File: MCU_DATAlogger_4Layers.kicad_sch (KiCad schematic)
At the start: 25 parts, among them U1 24LC1025, U2 24LC1025, U3 ATMEGA328P-AU, U4 DS1337S_, Y1 32.768KHz, Y2 16MHz

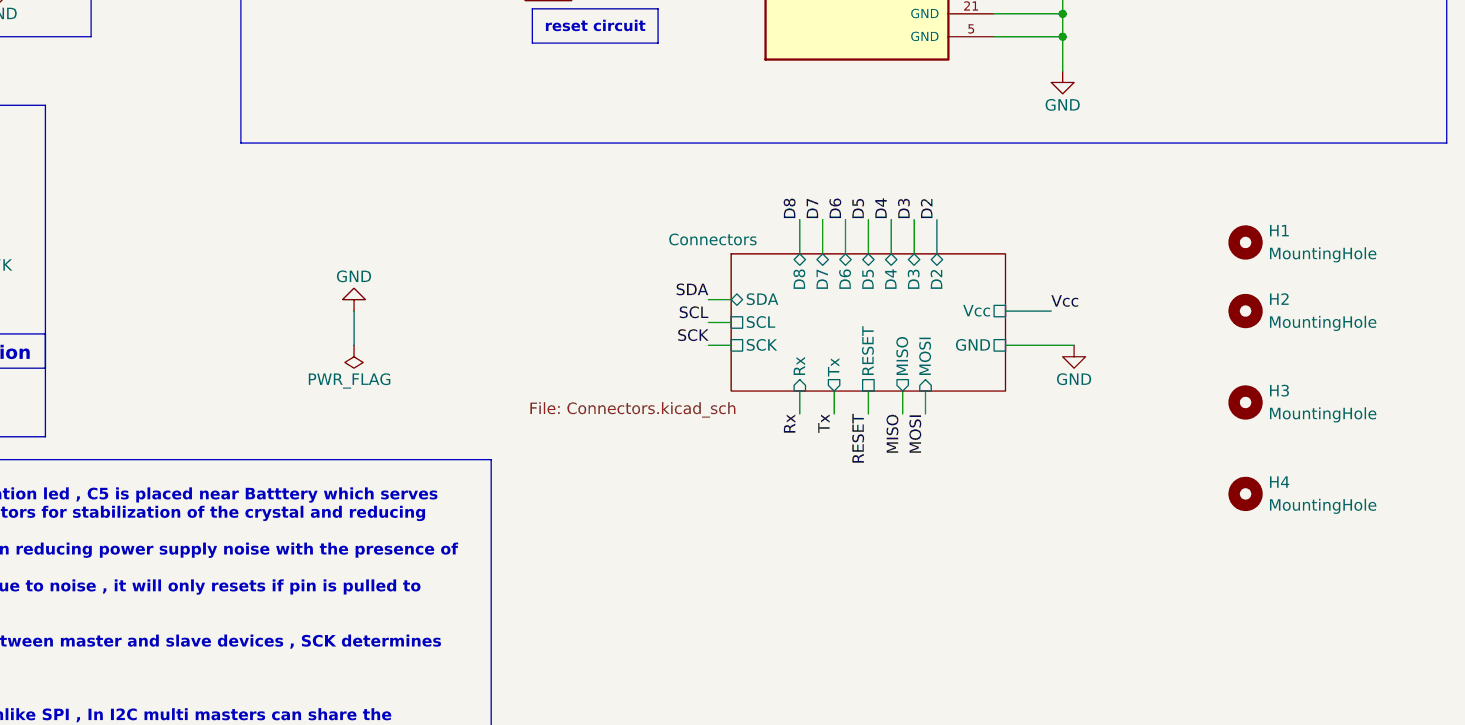
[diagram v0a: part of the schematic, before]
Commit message: Added a text box and some information on the page
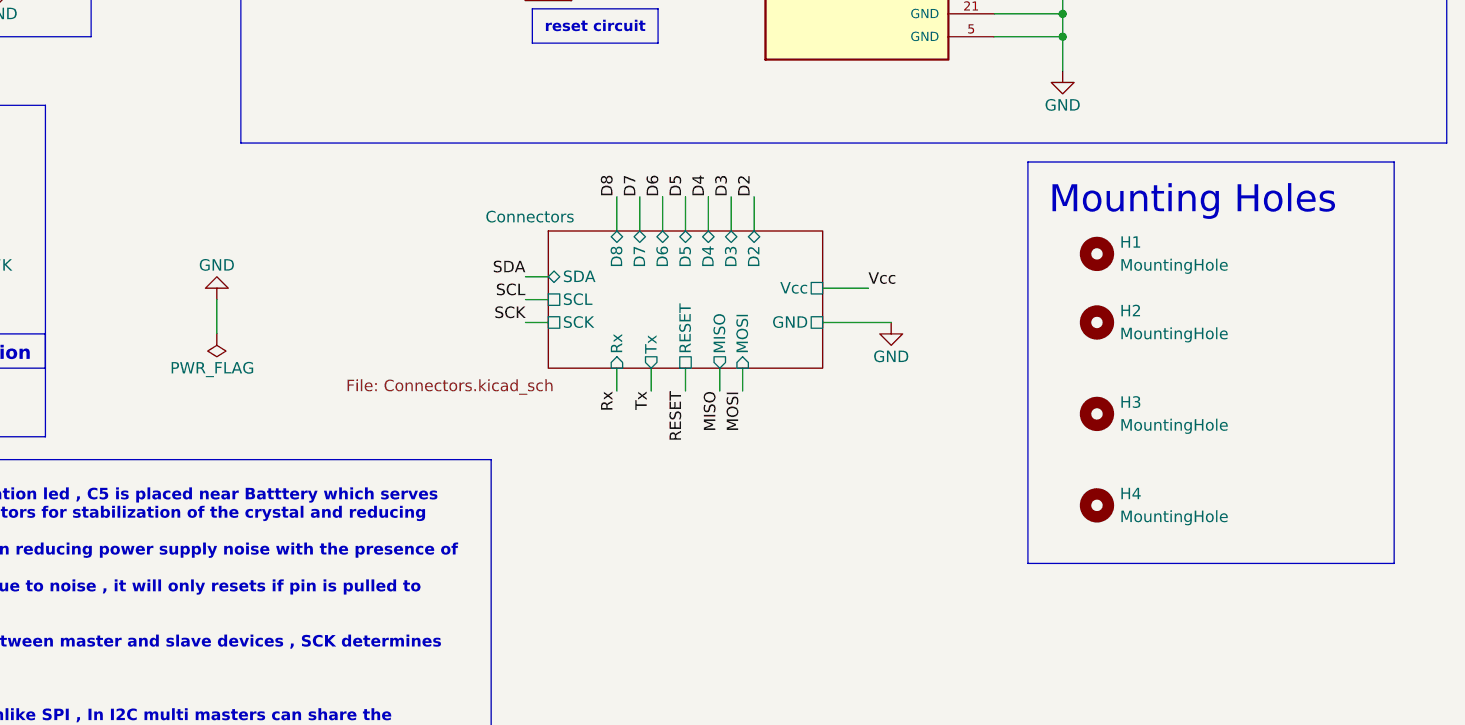
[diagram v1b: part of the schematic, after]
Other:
- company: (none) -> IMT SCHOOL
- title: (none) -> MCU DataLogger
- moved on the sheet: H1, H2, H3, H4
